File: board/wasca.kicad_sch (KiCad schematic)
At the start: 61 parts, among them CN1 CARTRIDGE_EDGE_CONNECTOR, CN2 TFP09-2-12B, CN3 Conn_02x02_Odd_Even, CN4 SODIMM-200, U1 74ALVC164245, U10 SN74LVC1T45DBV, U11 SN74LVC1T45DBV, U12 SN74LVC1T45DBV, U13 ESP32_CAM_HALF, U2 74ALVC164245, U3 MT48LC16M16A2TG, U4 LD1117S33TR_SOT223, U5 74ALVC164245, U8 SN74LVC1T45DBV, U9 SN74LVC1T45DBV

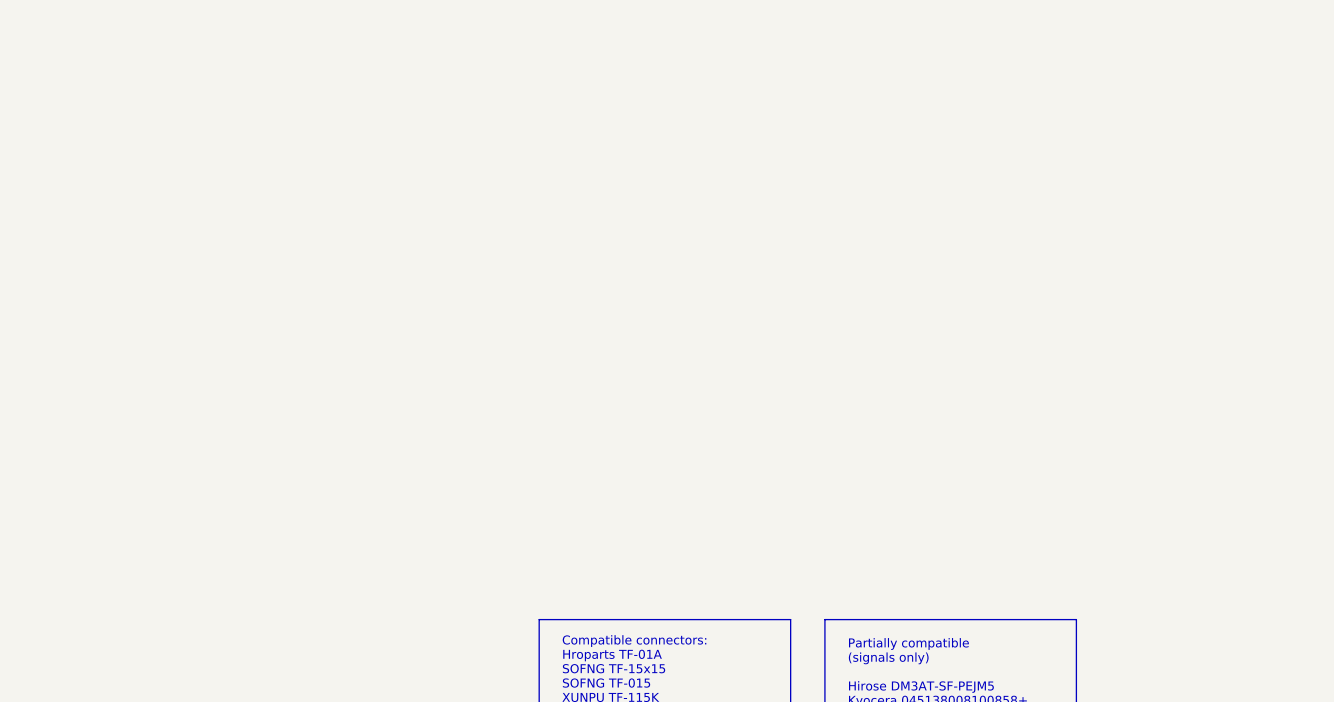
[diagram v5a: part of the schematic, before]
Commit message: Full SD card
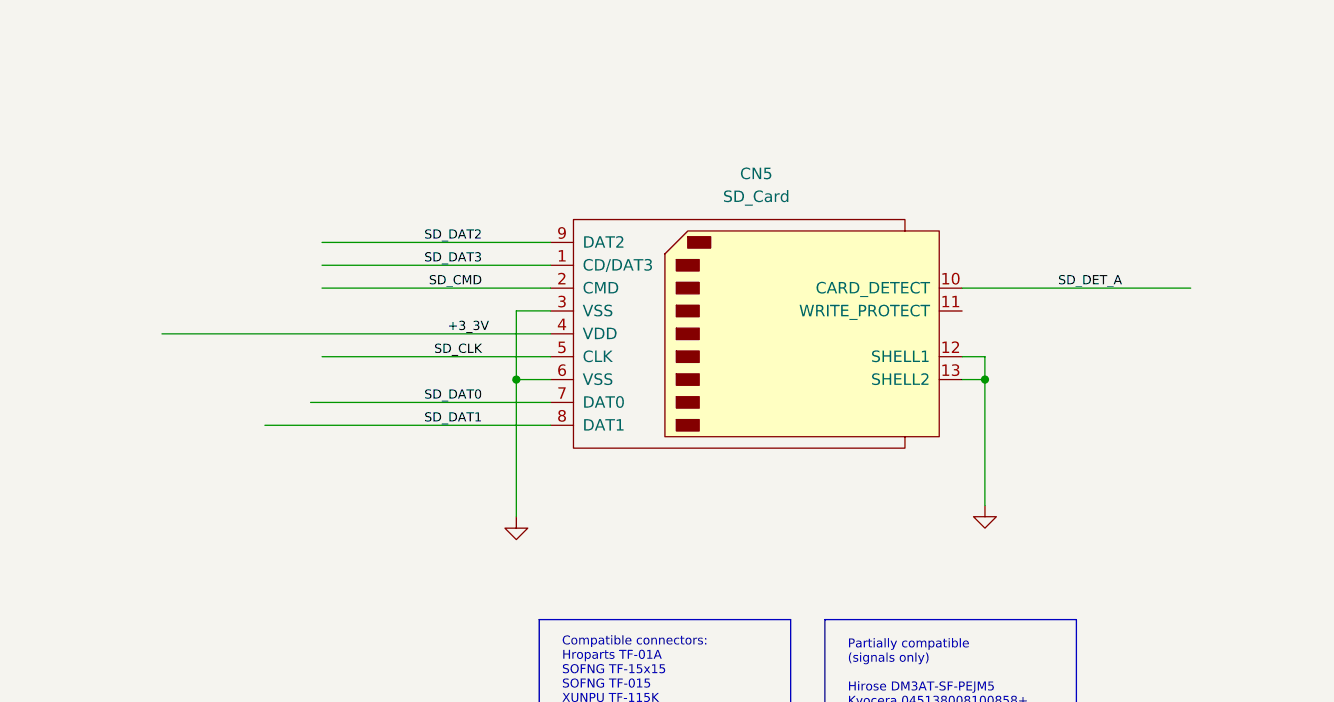
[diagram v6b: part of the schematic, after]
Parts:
- added CN5: SD_Card, Connector_Card:SD_Kyocera_145638009511859+, symbol Connector:SD_Card
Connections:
- net +3_3V: now also CN5.4 (VDD)
- net GND: now also CN5.12 (SHELL1), CN5.13 (SHELL2), CN5.3 (VSS), CN5.6 (VSS)
- net SD_CLK: now also CN5.5 (CLK)
- net SD_CMD: now also CN5.2 (CMD)
- net SD_DAT0: now also CN5.7 (DAT0)
- net SD_DAT1: now also CN5.8 (DAT1)
- net SD_DAT2: now also CN5.9 (DAT2)
- net SD_DAT3: now also CN5.1 (CD/DAT3)
- net SD_DET_A: now also CN5.10 (CARD_DETECT)
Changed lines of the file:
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@@
   (junction (at 640.08 204.47) (diameter 0) (color 0 0 0 0)
   )
+  (junction (at 796.29 379.73) (diameter 0) (color 0 0 0 0)
+  )
   (junction (at 240.03 116.84) (diameter 0) (color 0 0 0 0)
   )
@@
   (junction (at 99.06 110.49) (diameter 0) (color 0 0 0 0)
   )
+  (junction (at 744.22 379.73) (diameter 0) (color 0 0 0 0)
+  )
   (junction (at 138.43 218.44) (diameter 0) (color 0 0 0 0)
   )
@@
     (stroke (width 0) (type default) (color 0 0 0 0))
   )
+  (wire (pts (xy 722.63 364.49) (xy 748.03 364.49))
+    (stroke (width 0) (type default) (color 0 0 0 0))
+  )
   (wire (pts (xy 200.66 55.88) (xy 219.71 55.88))
     (stroke (width 0) (type default) (color 0 0 0 0))
@@
     (stroke (width 0) (type default) (color 0 0 0 0))
   )
+  (wire (pts (xy 748.03 372.11) (xy 744.22 372.11))
+    (stroke (width 0) (type default) (color 0 0 0 0))
+  )
   (wire (pts (xy 732.79 431.8) (xy 732.79 441.96))
     (stroke (width 0) (type default) (color 0 0 0 0))
@@
     (stroke (width 0) (type default) (color 0 0 0 0))
   )
+  (wire (pts (xy 744.22 379.73) (xy 744.22 394.97))
+    (stroke (width 0) (type default) (color 0 0 0 0))
+  )
   (wire (pts (xy 82.55 80.01) (xy 101.6 80.01))
     (stroke (width 0) (type default) (color 0 0 0 0))
@@
     (stroke (width 0) (type default) (color 0 0 0 0))
   )
+  (wire (pts (xy 744.22 372.11) (xy 744.22 379.73))
+    (stroke (width 0) (type default) (color 0 0 0 0))
+  )
   (wire (pts (xy 214.63 217.17) (xy 215.9 217.17))
     (stroke (width 0) (type default) (color 0 0 0 0))
@@
     (stroke (width 0) (type default) (color 0 0 0 0))
   )
+  (wire (pts (xy 716.28 384.81) (xy 748.03 384.81))
+    (stroke (width 0) (type default) (color 0 0 0 0))
+  )
   (wire (pts (xy 680.72 72.39) (xy 739.14 72.39))
     (stroke (width 0) (type default) (color 0 0 0 0))
@@
     (stroke (width 0) (type default) (color 0 0 0 0))
   )
+  (wire (pts (xy 793.75 379.73) (xy 796.29 379.73))
+    (stroke (width 0) (type default) (color 0 0 0 0))
+  )
   (wire (pts (xy 99.06 185.42) (xy 99.06 205.74))
     (stroke (width 0) (type default) (color 0 0 0 0))
@@
     (stroke (width 0) (type default) (color 0 0 0 0))
   )
+  (wire (pts (xy 722.63 369.57) (xy 748.03 369.57))
+    (stroke (width 0) (type default) (color 0 0 0 0))
+  )
   (wire (pts (xy 598.17 365.76) (xy 593.09 365.76))
     (stroke (width 0) (type default) (color 0 0 0 0))
@@
     (stroke (width 0) (type default) (color 0 0 0 0))
   )
+  (wire (pts (xy 793.75 369.57) (xy 819.15 369.57))
+    (stroke (width 0) (type default) (color 0 0 0 0))
+  )
   (wire (pts (xy 702.31 181.61) (xy 680.72 181.61))
     (stroke (width 0) (type default) (color 0 0 0 0))
@@
     (stroke (width 0) (type default) (color 0 0 0 0))
   )
+  (wire (pts (xy 793.75 377.19) (xy 796.29 377.19))
+    (stroke (width 0) (type default) (color 0 0 0 0))
+  )
   (wire (pts (xy 728.98 436.88) (xy 742.95 436.88))
     (stroke (width 0) (type default) (color 0 0 0 0))
@@
     (stroke (width 0) (type default) (color 0 0 0 0))
   )
+  (wire (pts (xy 796.29 379.73) (xy 796.29 393.7))
+    (stroke (width 0) (type default) (color 0 0 0 0))
+  )
   (wire (pts (xy 77.47 165.1) (xy 101.6 165.1))
     (stroke (width 0) (type default) (color 0 0 0 0))
@@
     (stroke (width 0) (type default) (color 0 0 0 0))
   )
+  (wire (pts (xy 796.29 377.19) (xy 796.29 379.73))
+    (stroke (width 0) (type default) (color 0 0 0 0))
+  )
   (wire (pts (xy 257.81 81.28) (xy 300.99 81.28))
     (stroke (width 0) (type default) (color 0 0 0 0))
@@
     (stroke (width 0) (type default) (color 0 0 0 0))
   )
+  (wire (pts (xy 722.63 367.03) (xy 748.03 367.03))
+    (stroke (width 0) (type default) (color 0 0 0 0))
+  )
   (wire (pts (xy 138.43 123.19) (xy 138.43 138.43))
     (stroke (width 0) (type default) (color 0 0 0 0))
@@
     (stroke (width 0) (type default) (color 0 0 0 0))
   )
+  (wire (pts (xy 722.63 377.19) (xy 748.03 377.19))
+    (stroke (width 0) (type default) (color 0 0 0 0))
+  )
   (wire (pts (xy 176.53 194.31) (xy 195.58 194.31))
     (stroke (width 0) (type default) (color 0 0 0 0))
@@
     (stroke (width 0) (type default) (color 0 0 0 0))
   )
+  (wire (pts (xy 744.22 379.73) (xy 748.03 379.73))
+    (stroke (width 0) (type default) (color 0 0 0 0))
+  )
   (wire (pts (xy 82.55 215.9) (xy 101.6 215.9))
     (stroke (width 0) (type default) (color 0 0 0 0))
@@
     (stroke (width 0) (type default) (color 0 0 0 0))
   )
+  (wire (pts (xy 704.85 374.65) (xy 748.03 374.65))
+    (stroke (width 0) (type default) (color 0 0 0 0))
+  )
   (wire (pts (xy 622.3 107.95) (xy 645.16 107.95))
     (stroke (width 0) (type default) (color 0 0 0 0))
@@
     (stroke (width 0) (type default) (color 0 0 0 0))
   )
+  (wire (pts (xy 721.36 382.27) (xy 748.03 382.27))
+    (stroke (width 0) (type default) (color 0 0 0 0))
+  )
   (image (at 585.47 532.13)
     (data
@@
     (effects (font (size 1.016 1.016)) (justify right bottom))
   )
+  (label "SD_DAT1" (at 740.41 384.81 180)
+    (effects (font (size 1.016 1.016)) (justify right bottom))
+  )
   (label "SDRAM_AUX_DQ1" (at 697.23 128.27 180)
     (effects (font (size 1.016 1.016)) (justify right bottom))
@@
     (effects (font (size 1.016 1.016)) (justify left bottom))
   )
+  (label "SD_DAT2" (at 740.41 364.49 180)
+    (effects (font (size 1.016 1.016)) (justify right bottom))
+  )
   (label "ABUS_D12" (at 181.61 325.12 0)
     (effects (font (size 1.016 1.016)) (justify left bottom))
@@
     (effects (font (size 1.016 1.016)) (justify right bottom))
   )
+  (label "+3_3V" (at 736.6 374.65 0)
+    (effects (font (size 1.016 1.016)) (justify left bottom))
+  )
   (label "ABUS_D11" (at 190.5 297.18 180)
     (effects (font (size 1.016 1.016)) (justify right bottom))
@@
     (effects (font (size 1.016 1.016)) (justify right bottom))
   )
+  (label "SD_DAT0" (at 740.41 382.27 180)
+    (effects (font (size 1.016 1.016)) (justify right bottom))
+  )
   (label "ABUS_3V_A15" (at 627.38 95.25 0)
     (effects (font (size 1.016 1.016)) (justify left bottom))
@@
     (effects (font (size 1.016 1.016)) (justify left bottom))
   )
+  (label "SD_CMD" (at 740.41 369.57 180)
+    (effects (font (size 1.016 1.016)) (justify right bottom))
+  )
   (label "SDRAM_AUX_A4" (at 697.23 189.23 180)
     (effects (font (size 1.016 1.016)) (justify right bottom))
@@
     (effects (font (size 1.016 1.016)) (justify right bottom))
   )
+  (label "SD_DAT3" (at 740.41 367.03 180)
+    (effects (font (size 1.016 1.016)) (justify right bottom))
+  )
   (label "ABUS_3V_A16" (at 626.11 158.75 0)
     (effects (font (size 1.016 1.016)) (justify left bottom))
@@
     (effects (font (size 1.016 1.016)) (justify right bottom))
   )
+  (label "SD_DET_A" (at 811.53 369.57 180)
+    (effects (font (size 1.016 1.016)) (justify right bottom))
+  )
   (label "RESET_3V" (at 262.89 99.06 0)
     (effects (font (size 1.016 1.016)) (justify left bottom))
@@
     (effects (font (size 1.016 1.016)) (justify left bottom))
   )
+  (label "SD_CLK" (at 740.41 377.19 180)
+    (effects (font (size 1.016 1.016)) (justify right bottom))
+  )
   (label "ABUS_3V_WR0" (at 262.89 53.34 0)
     (effects (font (size 1.016 1.016)) (justify left bottom))
@@
     (pin "9")
   )
+  (symbol (lib_id "power:GND") (at 796.29 393.7 0) (unit 1)
+    (in_bom yes) (on_board yes)
+    (property "Reference" "#PWR06" (id 0) (at 796.29 400.05 0)
+      (effects (font (size 1.27 1.27)) hide)
+    )
+    (property "Value" "GND" (id 1) (at 796.29 397.51 0)
+      (effects (font (size 1.27 1.27)) hide)
+    )
+    (property "Footprint" "" (id 2) (at 796.29 393.7 0)
+      (effects (font (size 1.524 1.524)))
+    )
+    (property "Datasheet" "" (id 3) (at 796.29 393.7 0)
+      (effects (font (size 1.524 1.524)))
+    )
+    (pin "1")
+  )
+  (symbol (lib_id "Connector:SD_Card") (at 770.89 374.65 0) (unit 1)
+    (in_bom yes) (on_board yes) (fields_autoplaced)
+    (property "Reference" "CN5" (id 0) (at 770.89 356.87 0))
+    (property "Value" "SD_Card" (id 1) (at 770.89 359.41 0))
+    (property "Footprint" "Connector_Card:SD_Kyocera_145638009511859+" (id 2) (at 770.89 374.65 0)
+      (effects (font (size 1.27 1.27)) hide)
+    )
+    (property "Datasheet" "http://portal.fciconnect.com/Comergent//fci/drawing/10067847.pdf" (id 3) (at 770.89 374.65 0)
+      (effects (font (size 1.27 1.27)) hide)
+    )
+    (pin "1")
+    (pin "10")
+    (pin "11")
+    (pin "12")
+    (pin "13")
+    (pin "2")
+    (pin "3")
+    (pin "4")
+    (pin "5")
+    (pin "6")
+    (pin "7")
+    (pin "8")
+    (pin "9")
+  )
+  (symbol (lib_id "power:GND") (at 744.22 394.97 0) (unit 1)
+    (in_bom yes) (on_board yes)
+    (property "Reference" "#PWR05" (id 0) (at 744.22 401.32 0)
+      (effects (font (size 1.27 1.27)) hide)
+    )
+    (property "Value" "GND" (id 1) (at 744.22 398.78 0)
+      (effects (font (size 1.27 1.27)) hide)
+    )
+    (property "Footprint" "" (id 2) (at 744.22 394.97 0)
+      (effects (font (size 1.524 1.524)))
+    )
+    (property "Datasheet" "" (id 3) (at 744.22 394.97 0)
+      (effects (font (size 1.524 1.524)))
+    )
+    (pin "1")
+  )
   (symbol (lib_id "power:GND") (at 739.14 82.55 0) (unit 1)
     (in_bom yes) (on_board yes)
@@
       (reference "#PWR04") (unit 1) (value "GND") (footprint "")
     )
+    (path "/bc26867e-2044-46bb-8920-dfb46ce37aad"
+      (reference "#PWR05") (unit 1) (value "GND") (footprint "")
+    )
+    (path "/8b39c82c-f2cd-4da6-952c-f37dbd2ef959"
+      (reference "#PWR06") (unit 1) (value "GND") (footprint "")
+    )
     (path "/00000000-0000-0000-0000-0000553adc89"
       (reference "#PWR018") (unit 1) (value "GND") (footprint "")
@@
       (reference "CN4") (unit 2) (value "SODIMM-200") (footprint "wasca:Conn_TE-DDR2-SODIMM-0.6-200P-doublesided")
     )
+    (path "/b1cbc4f0-17fb-4719-ab73-cd4b51a1994f"
+      (reference "CN5") (unit 1) (value "SD_Card") (footprint "Connector_Card:SD_Kyocera_145638009511859+")
+    )
     (path "/1abd061e-d5cc-4a20-af2d-482b0a0336a1"

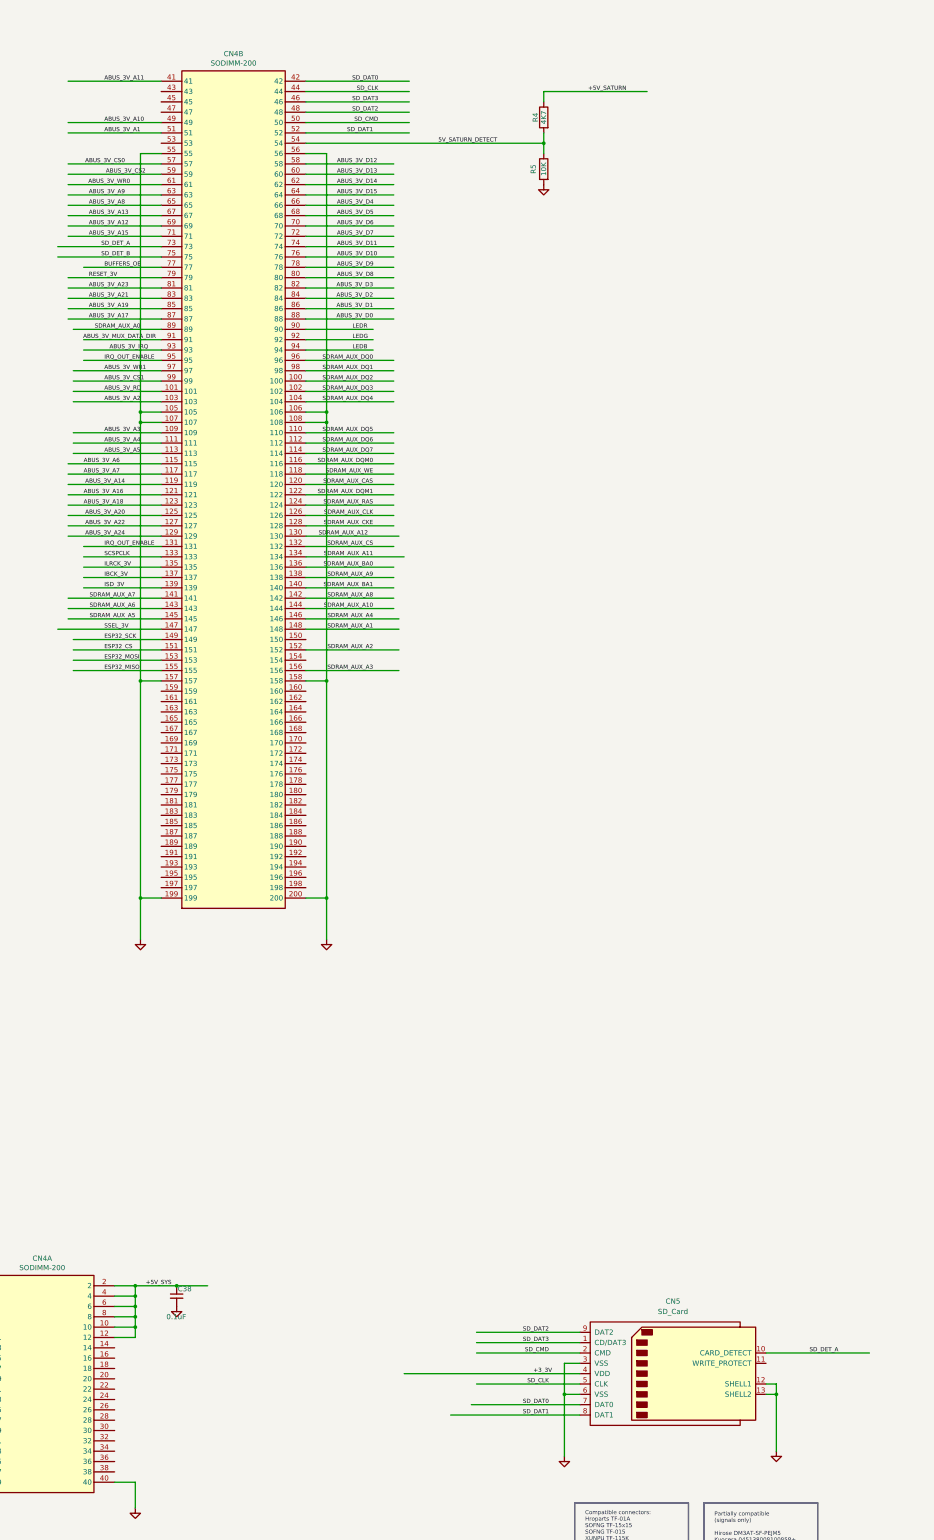
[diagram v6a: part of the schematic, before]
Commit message: Big SD connector
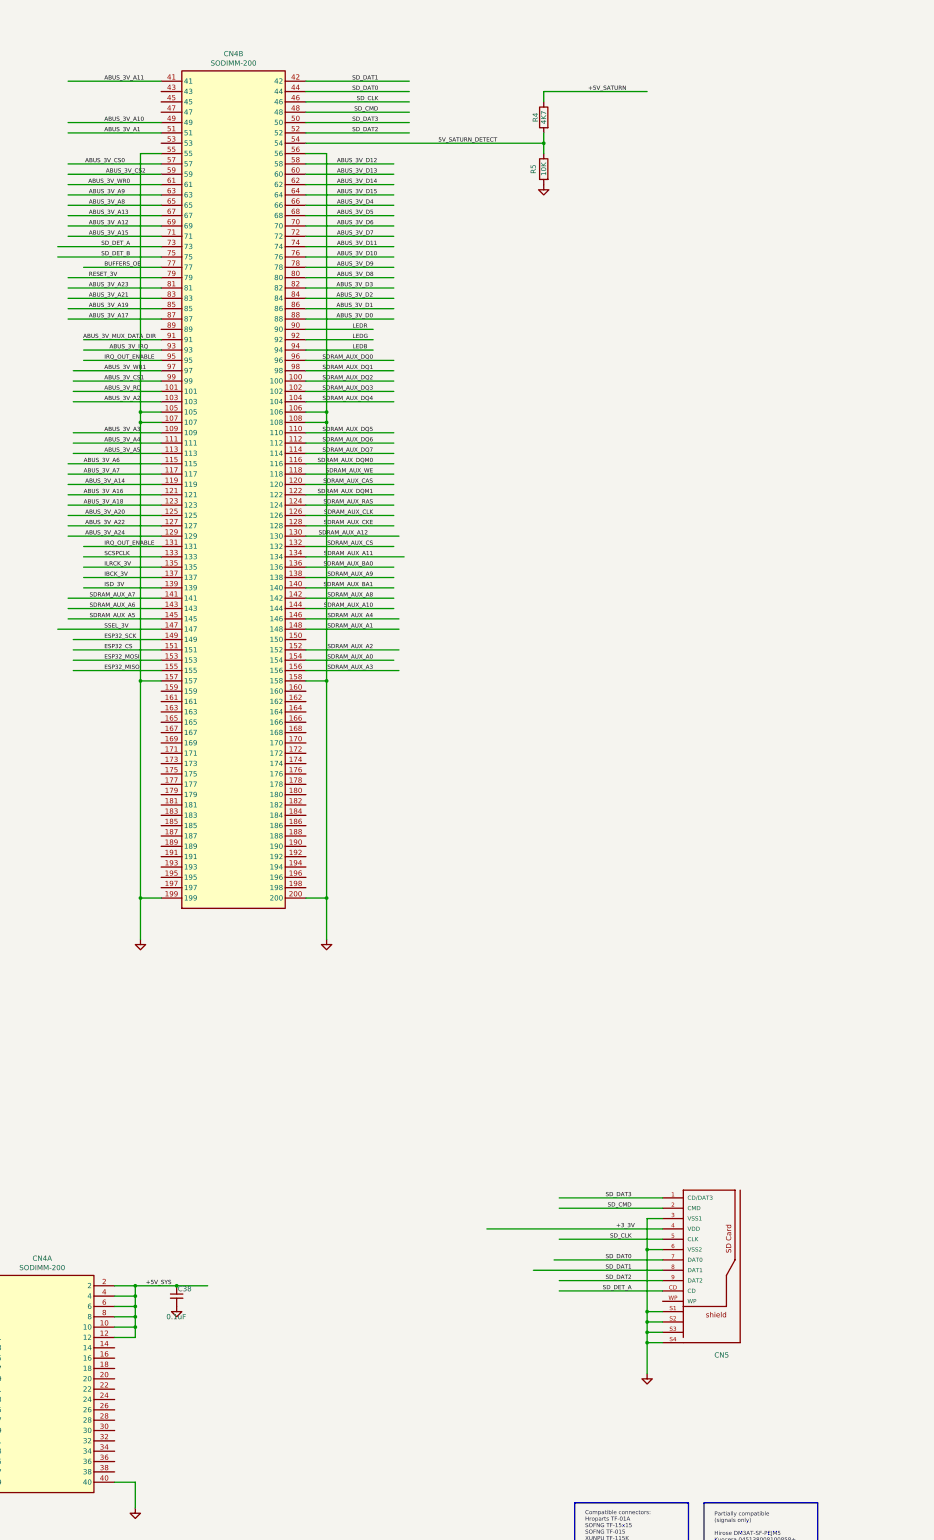
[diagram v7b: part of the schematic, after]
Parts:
- removed CN5: SD_Card, Connector_Card:SD_Kyocera_145638009511859+, symbol Connector:SD_Card
- added CN5: (no value), symbol 693063020911:693063020911
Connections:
- net +3_3V: now also CN5.4 (VDD)
- net GND: now also CN5.3 (VSS1), CN5.6 (VSS2), CN5.S1, CN5.S2, CN5.S3, CN5.S4; no longer CN4.89, U3.23 (A0)
- net SD_CLK: now also CN4.46, CN5.5 (CLK); no longer CN4.44
- net SD_CMD: now also CN4.48, CN5.2 (CMD); no longer CN4.50
- net SD_DAT0: now also CN4.44, CN5.7 (DAT0); no longer CN4.42
- net SD_DAT1: now also CN4.42, CN5.8 (DAT1); no longer CN4.52
- net SD_DAT2: now also CN4.52, CN5.9 (DAT2); no longer CN4.48
- net SD_DAT3: now also CN4.50, CN5.1 (CD/DAT3); no longer CN4.46
- net SD_DET_A: now also CN5.CD
- net SDRAM_AUX_A0: now reaches CN4.154
- net SDRAM_AUX_A0: now also U3.23 (A0)
